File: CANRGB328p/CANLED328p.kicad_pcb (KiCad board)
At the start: 2 copper layers, 86.5 x 65.5 mm, 30 parts, among them J1 Conn_01x06_Socket, J2 Conn_01x03_Socket, J3 AVR-ISP-6, U1 MCP2515-I_SO, U2 TSR_1-2450, U3 MCP2561-E_SN, U4 ATmega328-P, Y1 16 MHz, Y2 8 MHz

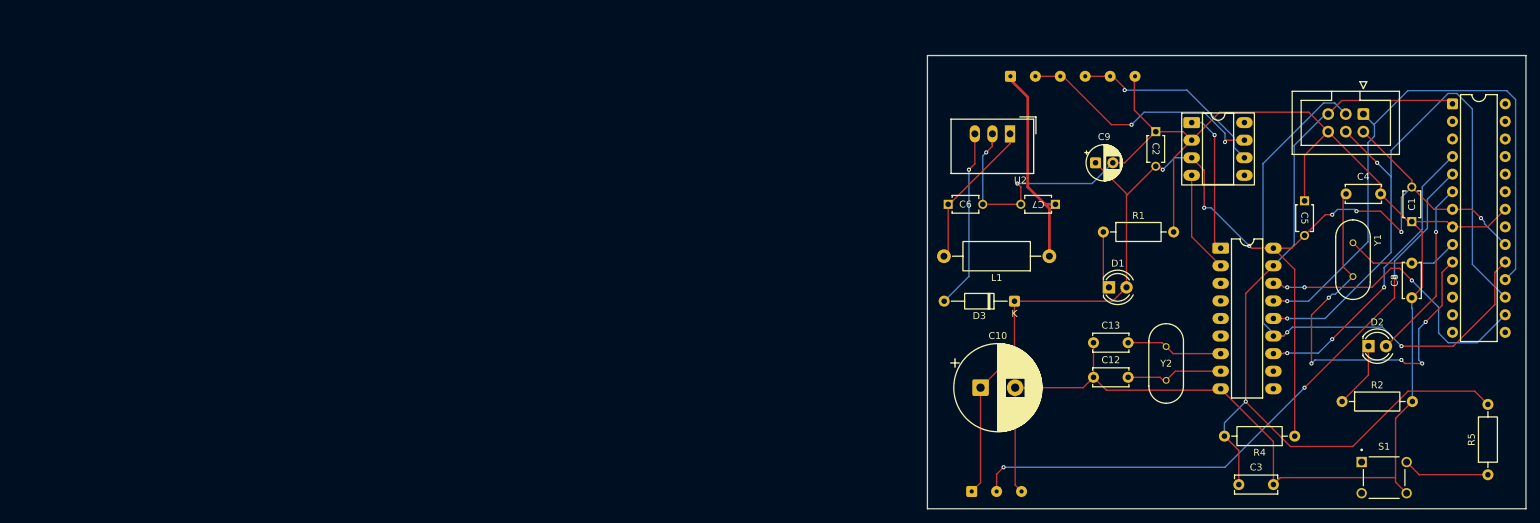
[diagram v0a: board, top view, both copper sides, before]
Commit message: Beginning of rev1 redesign - major error fixed
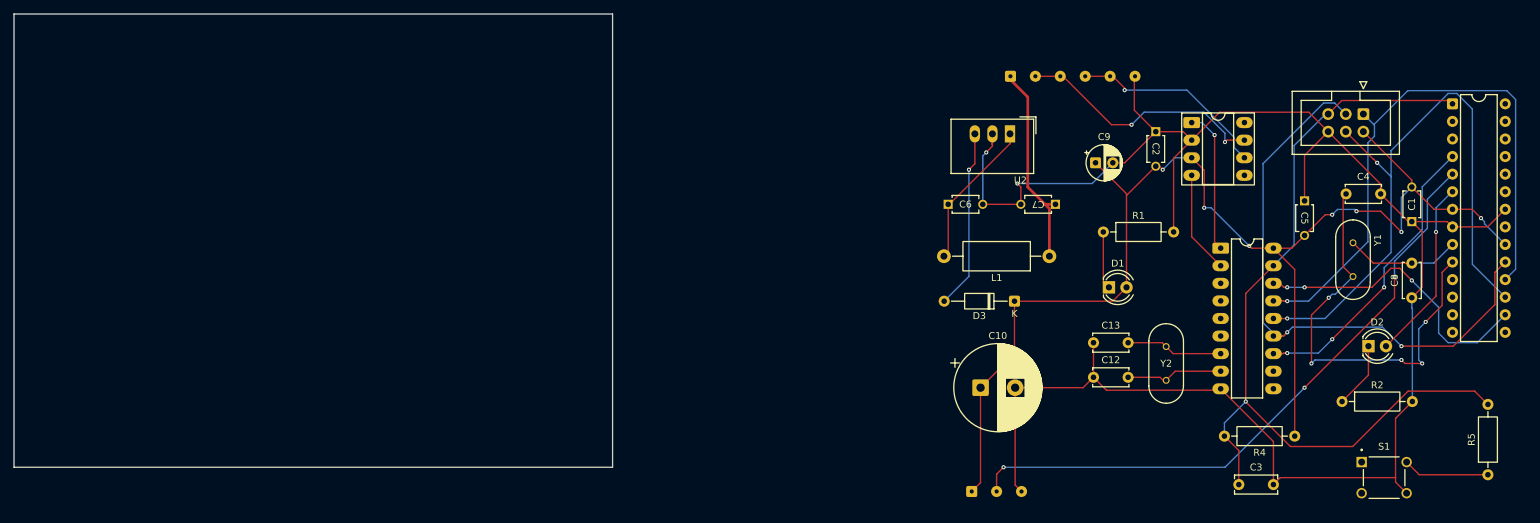
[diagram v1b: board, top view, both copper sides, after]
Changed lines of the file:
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@@
 	)
 	(gr_rect
-		(start 104.5 28)
-		(end 191 93.5)
+		(start -27.5 22)
+		(end 59 87.5)
 		(stroke
 			(width 0.05)
